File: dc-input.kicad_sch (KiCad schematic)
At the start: 4 parts, among them J11 DC_SOCKET

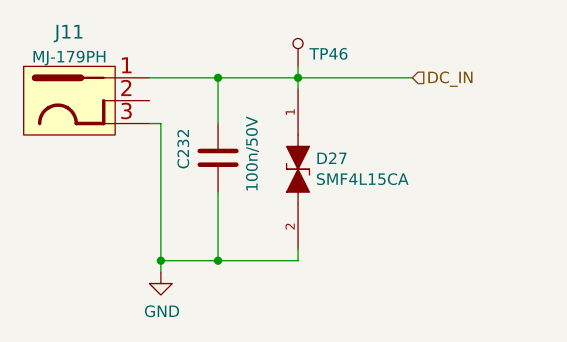
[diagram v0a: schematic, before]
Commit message: Added cosmetic changes to schematics (e.g. position of labels, designators)
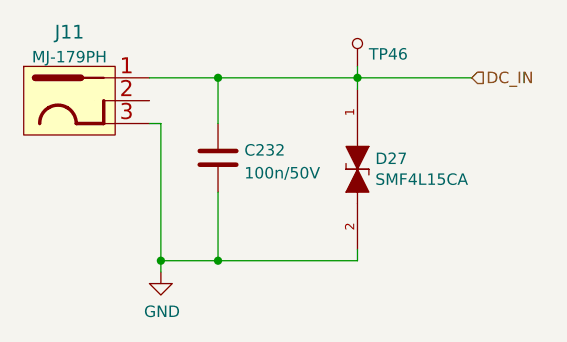
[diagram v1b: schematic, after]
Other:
- moved on the sheet: D27, TP46
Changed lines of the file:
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@@
   (junction (at 152.4 109.22) (diameter 0) (color 0 0 0 0)
   )
-  (junction (at 161.29 88.9) (diameter 0) (color 0 0 0 0)
+  (junction (at 167.894 88.9) (diameter 0) (color 0 0 0 0)
   )
   (junction (at 146.05 109.22) (diameter 0) (color 0 0 0 0)
@@
   (junction (at 152.4 88.9) (diameter 0) (color 0 0 0 0)
   )
-  (wire (pts (xy 152.4 88.9) (xy 161.29 88.9))
+  (wire (pts (xy 152.4 88.9) (xy 167.894 88.9))
     (stroke (width 0) (type default) (color 0 0 0 0))
   )
@@
     (stroke (width 0) (type default) (color 0 0 0 0))
   )
-  (wire (pts (xy 152.4 109.22) (xy 161.29 109.22))
+  (wire (pts (xy 152.4 109.22) (xy 167.894 109.22))
     (stroke (width 0) (type default) (color 0 0 0 0))
   )
@@
     (stroke (width 0) (type default) (color 0 0 0 0))
   )
-  (wire (pts (xy 161.29 88.9) (xy 173.99 88.9))
+  (wire (pts (xy 167.894 88.9) (xy 180.594 88.9))
     (stroke (width 0) (type default) (color 0 0 0 0))
   )
@@
     (stroke (width 0) (type default) (color 0 0 0 0))
   )
-  (wire (pts (xy 161.29 88.9) (xy 161.29 87.63))
+  (wire (pts (xy 167.894 88.9) (xy 167.894 87.63))
     (stroke (width 0) (type default) (color 0 0 0 0))
   )
-  (wire (pts (xy 161.29 90.17) (xy 161.29 88.9))
+  (wire (pts (xy 167.894 90.17) (xy 167.894 88.9))
     (stroke (width 0) (type default) (color 0 0 0 0))
   )
@@
     (stroke (width 0) (type default) (color 0 0 0 0))
   )
-  (wire (pts (xy 161.29 107.95) (xy 161.29 109.22))
+  (wire (pts (xy 167.894 107.95) (xy 167.894 109.22))
     (stroke (width 0) (type default) (color 0 0 0 0))
   )
@@
     )
   )
-  (hierarchical_label "DC_IN" (shape input) (at 173.99 88.9 0)
+  (hierarchical_label "DC_IN" (shape input) (at 180.594 88.9 0)
     (effects (font (size 1.27 1.27)) (justify left))
   )
-  (symbol (lib_id "kria-k26-devboard:SMF4L15CA") (at 161.29 99.06 270) (unit 1)
+  (symbol (lib_id "kria-k26-devboard:SMF4L15CA") (at 167.894 99.06 270) (unit 1)
     (in_bom yes) (on_board yes)
-    (property "Reference" "D27" (id 0) (at 163.2712 97.8916 90)
+    (property "Reference" "D27" (id 0) (at 169.8752 97.8916 90)
       (effects (font (size 1.27 1.27)) (justify left))
     )
-    (property "Value" "SMF4L15CA" (id 1) (at 163.2712 100.203 90)
+    (property "Value" "SMF4L15CA" (id 1) (at 169.8752 100.203 90)
       (effects (font (size 1.27 1.27)) (justify left))
     )
-    (property "Footprint" "kria-k26-devboard-footprints:SOD-123FL" (id 2) (at 161.29 99.06 0)
+    (property "Footprint" "kria-k26-devboard-footprints:SOD-123FL" (id 2) (at 167.894 99.06 0)
       (effects (font (size 1.27 1.27)) hide)
     )
-    (property "Datasheet" "https://www.mouser.pl/datasheet/2/240/Littelfuse_TVS_Diode_SMF4L_Datasheet_pdf-1665786.pdf" (id 3) (at 161.29 99.06 0)
+    (property "Datasheet" "https://www.mouser.pl/datasheet/2/240/Littelfuse_TVS_Diode_SMF4L_Datasheet_pdf-1665786.pdf" (id 3) (at 167.894 99.06 0)
       (effects (font (size 1.27 1.27)) hide)
     )
-    (property "MPN" "SMF4L15CA" (id 4) (at 161.29 99.06 0)
+    (property "MPN" "SMF4L15CA" (id 4) (at 167.894 99.06 0)
       (effects (font (size 1.27 1.27)) hide)
     )
-    (property "Manufacturer" "Infineon Technologies" (id 5) (at 161.29 99.06 0)
+    (property "Manufacturer" "Infineon Technologies" (id 5) (at 167.894 99.06 0)
       (effects (font (size 1.27 1.27)) hide)
     )
@@
   )
   (symbol (lib_id "kria-k26-devboard:C_100n_0402_50V") (at 152.4 97.79 0) (unit 1)
-    (in_bom yes) (on_board yes)
-    (property "Reference" "C232" (id 0) (at 148.59 99.06 90)
+    (in_bom yes) (on_board yes) (fields_autoplaced)
+    (property "Reference" "C232" (id 0) (at 155.321 96.9553 0)
       (effects (font (size 1.27 1.27)) (justify left))
     )
@@
       (effects (font (size 1.27 1.27)) hide)
     )
-    (property "Val" "100n/50V" (id 6) (at 156.21 101.6 90)
+    (property "Val" "100n/50V" (id 6) (at 155.321 99.4922 0)
       (effects (font (size 1.27 1.27)) (justify left))
     )
@@
     (pin "2")
   )
-  (symbol (lib_id "kria-k26-devboard:TP_SMD_0_75MM") (at 161.29 85.09 180) (unit 1)
+  (symbol (lib_id "kria-k26-devboard:TP_SMD_0_75MM") (at 167.894 85.09 180) (unit 1)
     (in_bom yes) (on_board yes)
-    (property "Reference" "TP46" (id 0) (at 162.56 86.2838 0)
+    (property "Reference" "TP46" (id 0) (at 169.164 86.2838 0)
       (effects (font (size 1.27 1.27)) (justify right))
     )
-    (property "Value" "TP_SMD_0_75MM" (id 1) (at 161.29 82.55 0)
+    (property "Value" "TP_SMD_0_75MM" (id 1) (at 167.894 82.55 0)
       (effects (font (size 1.27 1.27)) hide)
     )
-    (property "Footprint" "kria-k26-devboard-footprints:Testpoint_smd_0_75mm" (id 2) (at 156.21 90.17 0)
+    (property "Footprint" "kria-k26-devboard-footprints:Testpoint_smd_0_75mm" (id 2) (at 162.814 90.17 0)
       (effects (font (size 1.524 1.524)) (justify left) hide)
     )
-    (property "Datasheet" "" (id 3) (at 156.21 92.71 0)
+    (property "Datasheet" "" (id 3) (at 162.814 92.71 0)
       (effects (font (size 1.524 1.524)) (justify left) hide)
     )

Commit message: Bump date and revision
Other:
- title: DC Jack  -> Kria K26 Devboard
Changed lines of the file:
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@@
   (paper "A4")
   (title_block
-    (title "DC Jack ")
-    (date "2022-07-25")
-    (rev "1.1.0")
+    (title "Kria K26 Devboard")
+    (date "2023-02-15")
+    (rev "1.1.1")
     (comment 1 "www.antmicro.com")
     (comment 2 "Antmicro Ltd.")

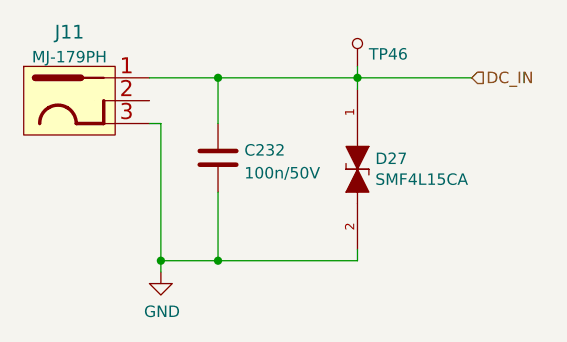
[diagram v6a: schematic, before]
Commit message: Replace FTDI 3V3 Regulator
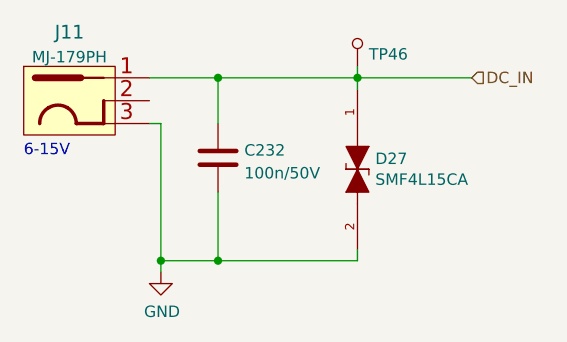
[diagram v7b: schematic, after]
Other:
- note added: "6-15V"
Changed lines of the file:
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@@
     )
+  )
+  (text "6-15V" (at 130.81 97.79 0)
+    (effects (font (size 1.27 1.27)) (justify left bottom))
   )
   (hierarchical_label "DC_IN" (shape input) (at 180.594 88.9 0)
